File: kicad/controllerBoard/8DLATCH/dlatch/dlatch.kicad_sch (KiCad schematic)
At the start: 12 parts, among them Q289 PMOS, Q290 NMOS, Q291 PMOS, Q292 NMOS, Q293 PMOS, Q294 NMOS, Q295 PMOS, Q296 NMOS, Q297 PMOS, Q298 NMOS, Q299 PMOS, Q300 NMOS

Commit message: Finish input stage schematic
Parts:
- renumbered Q289 to Q71, Q290 to Q72, Q291 to Q73, Q292 to Q74, Q293 to Q75, Q294 to Q76, Q295 to Q77, Q296 to Q78, Q297 to Q79, Q298 to Q80, Q299 to Q81, Q300 to Q82

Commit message: did stuff
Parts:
- renumbered Q71 to Q72, Q72 to Q73, Q73 to Q74, Q74 to Q75, Q75 to Q76, Q76 to Q77, Q77 to Q78, Q78 to Q79, Q79 to Q80, Q80 to Q81, Q81 to Q82, Q82 to Q83

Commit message: did more simulation, added bom
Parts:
- renumbered Q72 to Q71, Q73 to Q72, Q74 to Q73, Q75 to Q74, Q76 to Q75, Q77 to Q76, Q78 to Q77, Q79 to Q78, Q80 to Q79, Q81 to Q80, Q82 to Q81, Q83 to Q82

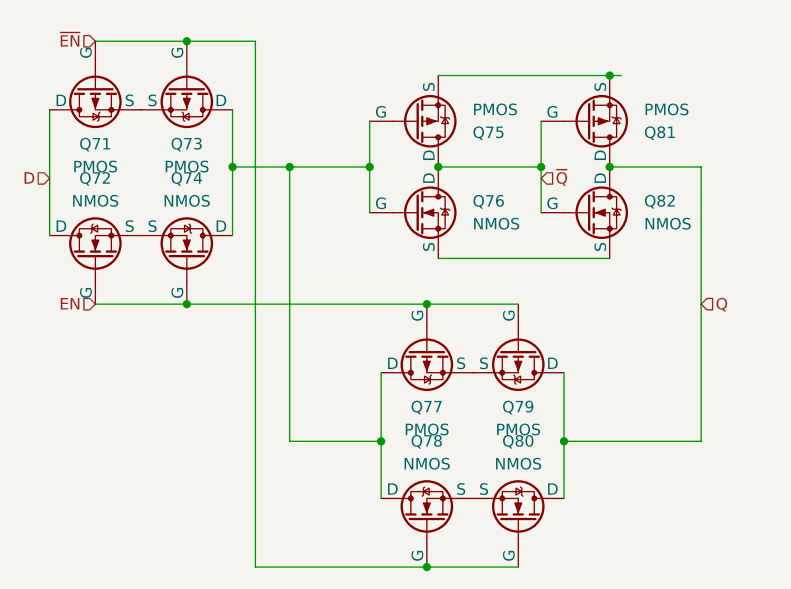
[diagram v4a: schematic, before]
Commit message: update main board schematic
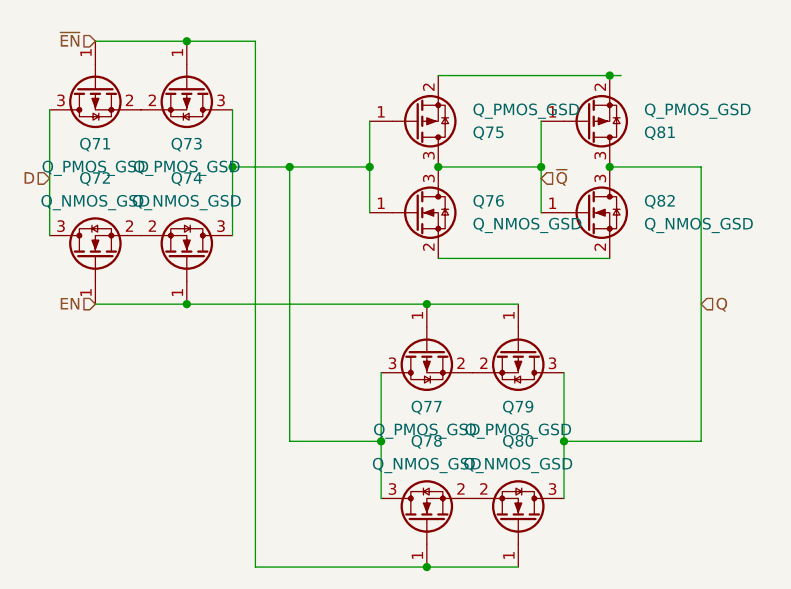
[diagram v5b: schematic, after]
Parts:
- Q71, Q73, Q75, Q77, Q79, Q81: value PMOS -> Q_PMOS_GSD; footprint (none) -> easyeda2kicad:SOT-23-P; symbol Simulation_SPICE:PMOS -> Transistor_FET:Q_PMOS_GSD
- Q72, Q74, Q76, Q78, Q80, Q82: value NMOS -> Q_NMOS_GSD; footprint (none) -> easyeda2kicad:SOT-23-N; symbol Simulation_SPICE:NMOS -> Transistor_FET:Q_NMOS_GSD
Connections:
- net D: now also Q71.3 (D), Q72.3 (D); no longer Q71.1 (D), Q72.1 (D)
- net EN: now also Q72.1 (G), Q74.1 (G), Q77.1 (G), Q79.1 (G); no longer Q72.2 (G), Q74.2 (G), Q77.2 (G), Q79.2 (G)
- net Q: now also Q79.3 (D), Q80.3 (D), Q81.3 (D), Q82.3 (D); no longer Q79.1 (D), Q80.1 (D), Q81.1 (D), Q82.1 (D)
- net ~{EN}: now also Q71.1 (G), Q73.1 (G), Q78.1 (G), Q80.1 (G); no longer Q71.2 (G), Q73.2 (G), Q78.2 (G), Q80.2 (G)
- net ~{Q}: now also Q75.3 (D), Q76.3 (D), Q81.1 (G), Q82.1 (G); no longer Q75.1 (D), Q76.1 (D), Q81.2 (G), Q82.2 (G)
- net at Q73.3 (D): now also Q74.3 (D), Q75.1 (G), Q76.1 (G), Q77.3 (D), Q78.3 (D); no longer Q71.3 (S)
- new net: Q71.2 (S), Q73.2 (S)
- new net: Q78.2 (S), Q80.2 (S)
- new net: Q77.2 (S), Q79.2 (S)
- new net: Q72.2 (S), Q74.2 (S)
- new net: Q75.2 (S), Q81.2 (S)
- new net: Q76.2 (S), Q82.2 (S)

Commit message: continue routing main controller board
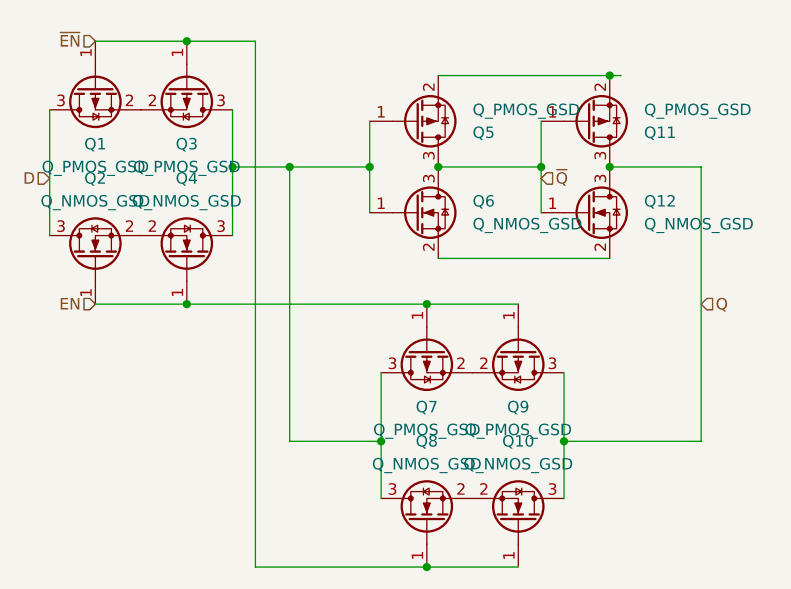
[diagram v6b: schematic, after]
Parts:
- renumbered Q71 to Q1, Q80 to Q10, Q81 to Q11, Q82 to Q12, Q72 to Q2, Q73 to Q3, Q74 to Q4, Q75 to Q5, Q76 to Q6, Q77 to Q7, Q78 to Q8, Q79 to Q9

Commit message: finished routing all sub schematics
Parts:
- renumbered Q1 to Q71, Q2 to Q72, Q3 to Q73, Q4 to Q74, Q5 to Q75, Q6 to Q76, Q7 to Q77, Q8 to Q78, Q9 to Q79, Q10 to Q80, Q11 to Q81, Q12 to Q82
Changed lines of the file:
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@@
 		(in_pos_files yes)
 		(dnp no)
-		(property "Reference" "Q1"
+		(property "Reference" "Q71"
 			(at 62.23 57.15 90)
 			(show_name no)
@@
 		(dnp no)
 		(fields_autoplaced yes)
-		(property "Reference" "Q8"
+		(property "Reference" "Q78"
 			(at 99.06 90.17 90)
 			(show_name no)
@@
 		(dnp no)
 		(fields_autoplaced yes)
-		(property "Reference" "Q3"
+		(property "Reference" "Q73"
 			(at 72.39 57.15 90)
 			(show_name no)
@@
 		(dnp no)
 		(fields_autoplaced yes)
-		(property "Reference" "Q9"
+		(property "Reference" "Q79"
 			(at 109.22 86.36 90)
 			(show_name no)
@@
 		(dnp no)
 		(fields_autoplaced yes)
-		(property "Reference" "Q2"
+		(property "Reference" "Q72"
 			(at 62.23 60.96 90)
 			(show_name no)
@@
 		(in_pos_files yes)
 		(dnp no)
-		(property "Reference" "Q7"
+		(property "Reference" "Q77"
 			(at 99.06 86.36 90)
 			(show_name no)
@@
 		(in_pos_files yes)
 		(dnp no)
-		(property "Reference" "Q5"
+		(property "Reference" "Q75"
 			(at 104.14 55.8801 0)
 			(show_name no)
@@
 		(dnp no)
 		(fields_autoplaced yes)
-		(property "Reference" "Q12"
+		(property "Reference" "Q82"
 			(at 123.19 63.4999 0)
 			(show_name no)
@@
 		(in_pos_files yes)
 		(dnp no)
-		(property "Reference" "Q10"
+		(property "Reference" "Q80"
 			(at 109.22 90.17 90)
 			(show_name no)
@@
 		(in_pos_files yes)
 		(dnp no)
-		(property "Reference" "Q4"
+		(property "Reference" "Q74"
 			(at 72.39 60.96 90)
 			(show_name no)
@@
 		(dnp no)
 		(fields_autoplaced yes)
-		(property "Reference" "Q6"
+		(property "Reference" "Q76"
 			(at 104.14 63.4999 0)
 			(show_name no)
@@
 		(in_pos_files yes)
 		(dnp no)
-		(property "Reference" "Q11"
+		(property "Reference" "Q81"
 			(at 123.19 55.8801 0)
 			(show_name no)

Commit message: add mounting holes
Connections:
- net +5V: now reaches Q75.2 (S), Q81.2 (S)
- net GND: now reaches Q76.2 (S), Q82.2 (S)
